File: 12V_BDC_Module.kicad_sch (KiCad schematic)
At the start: 18 parts, among them J1 Conn_01x10_Pin, J2 Conn_01x10_Pin, J4 Conn_01x10_Pin, U1 TPS54531DDA

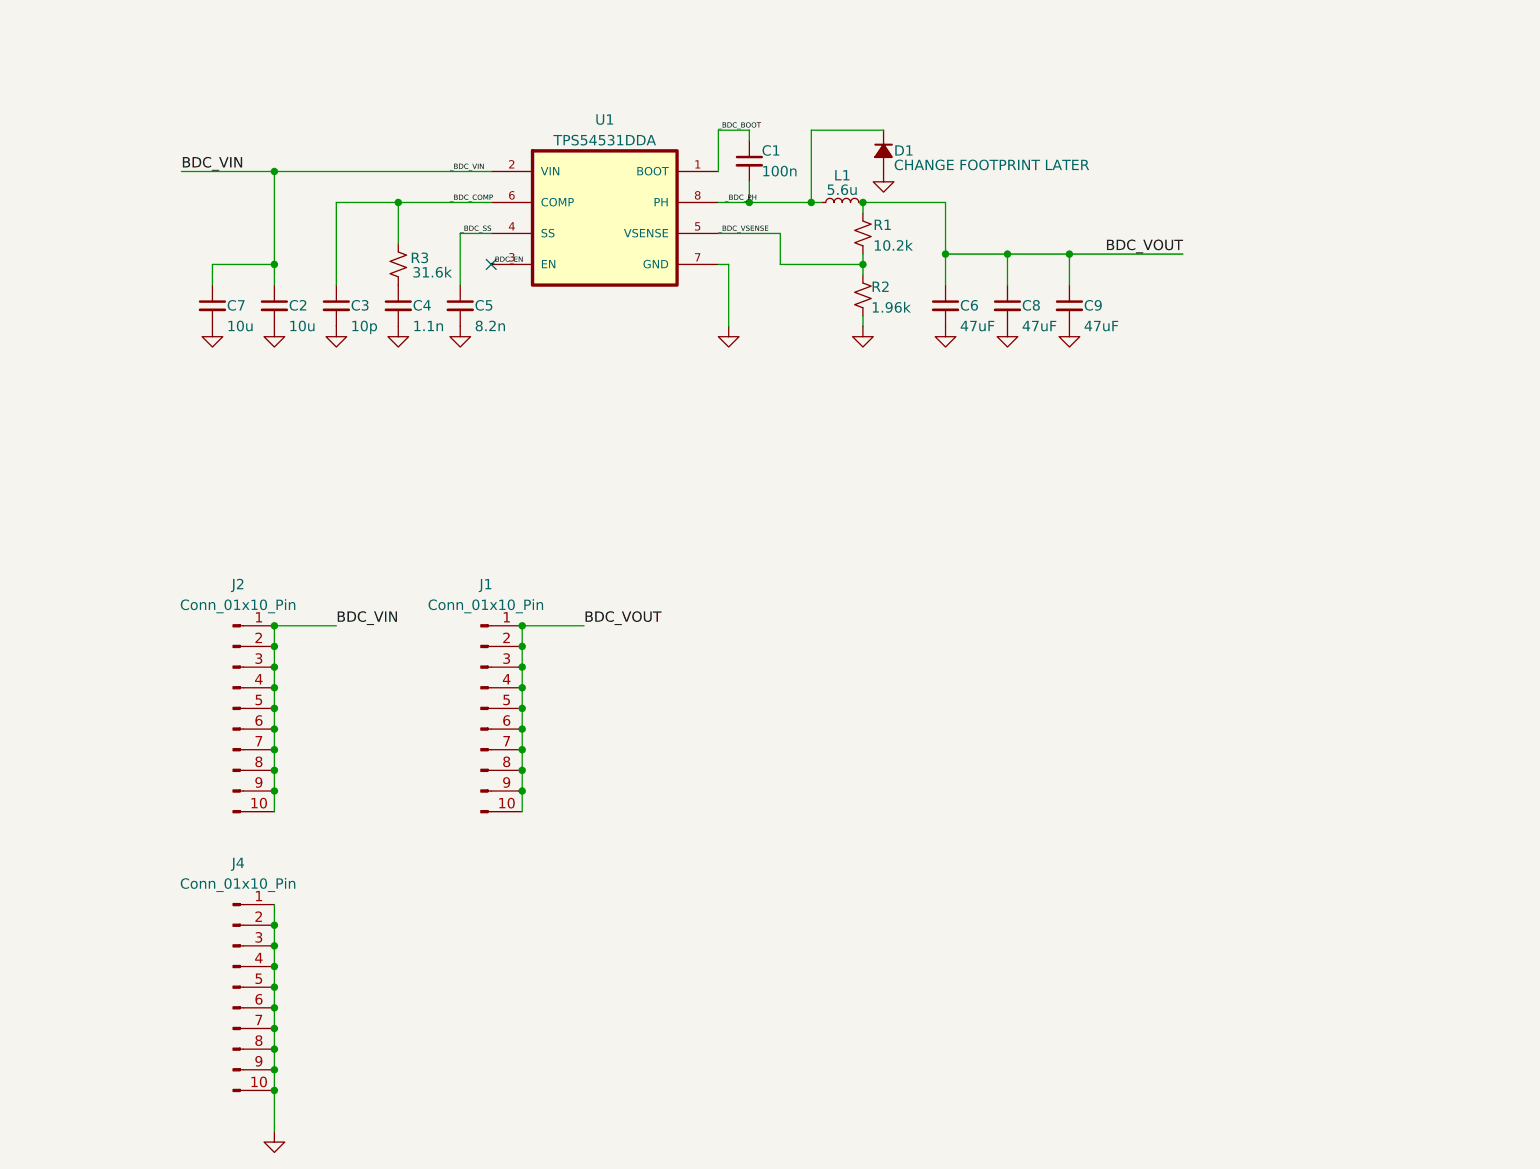
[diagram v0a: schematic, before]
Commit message: Organize, make BDC Module more solderable
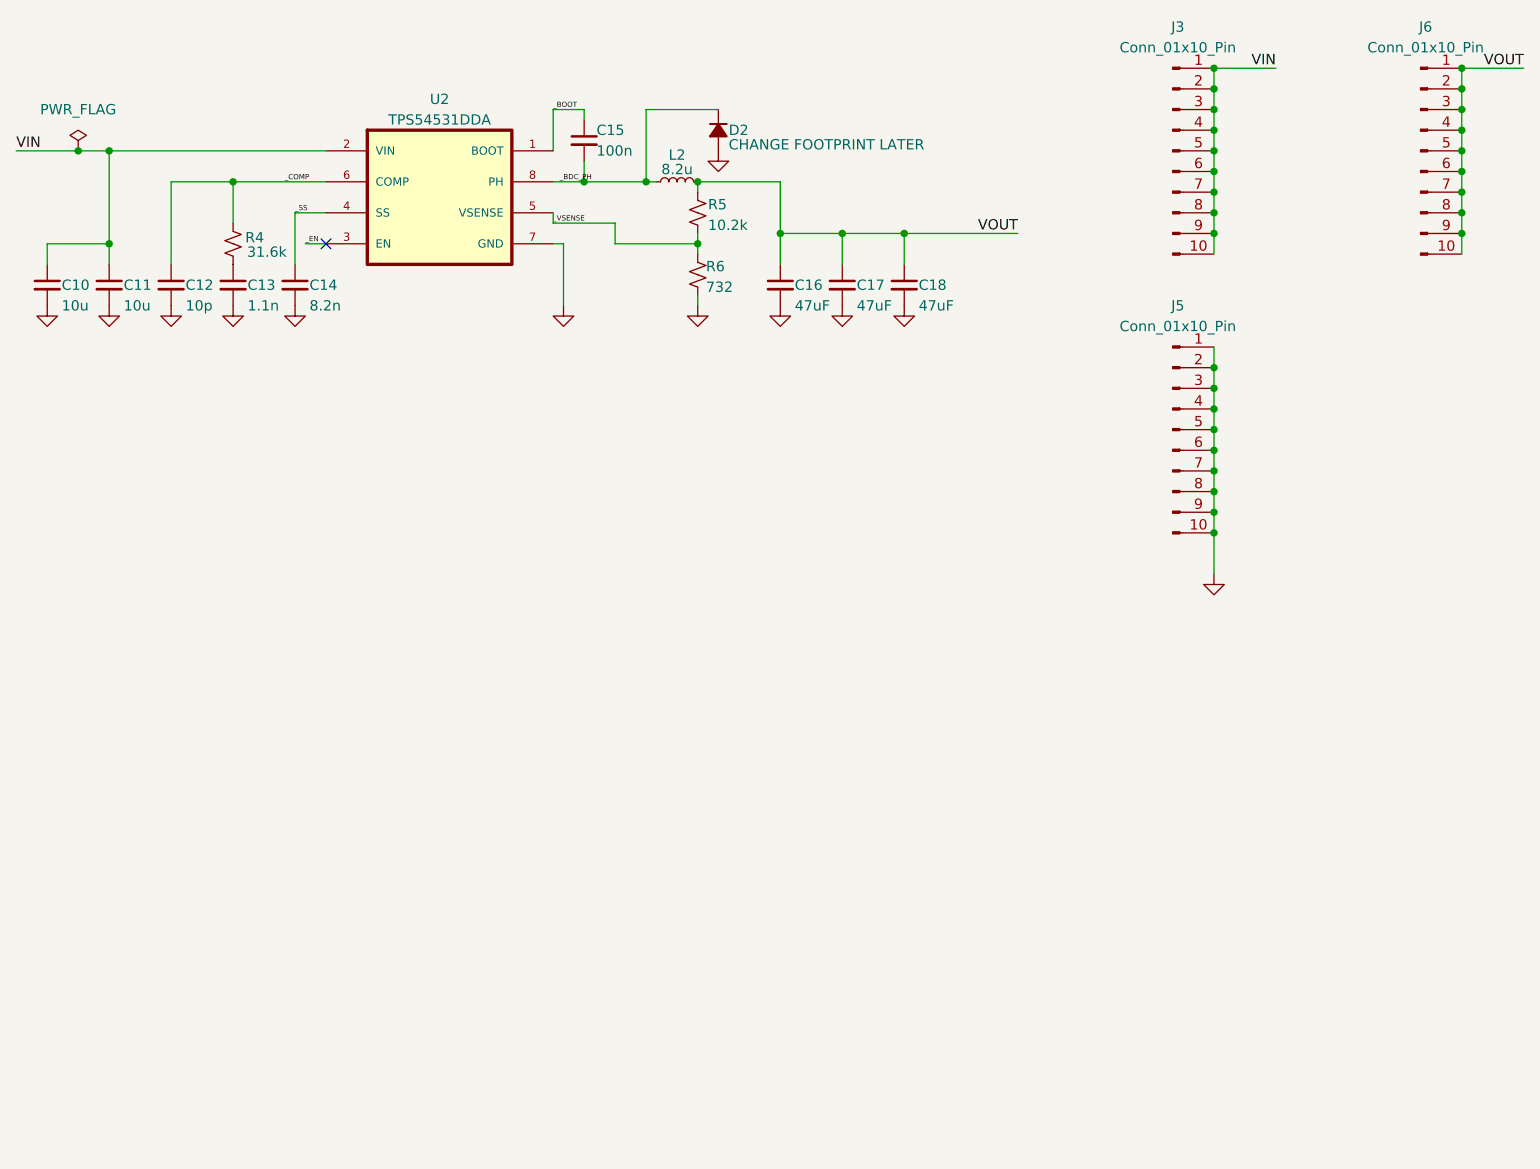
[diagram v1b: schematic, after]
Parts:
- removed C1: 100n, Capacitor_SMD:C_0805_2012Metric, symbol Device:C_Small
- removed C2, C7: 10u, Capacitor_SMD:C_0805_2012Metric, symbol Device:C_Small
- removed C3: 10p, Capacitor_SMD:C_0805_2012Metric, symbol Device:C_Small
- removed C4: 1.1n, Capacitor_SMD:C_0805_2012Metric, symbol Device:C_Small
- removed C5: 8.2n, Capacitor_SMD:C_0805_2012Metric, symbol Device:C_Small
- removed C6, C8, C9: 47uF, Capacitor_SMD:C_0805_2012Metric, symbol Device:C_Small
- removed D1: CHANGE FOOTPRINT LATER, Diode_SMD:D_0805_2012Metric, symbol Device:D_Small_Filled
- removed J1, J2, J4: Conn_01x10_Pin, Connector_PinHeader_2.54mm:PinHeader_1x10_P2.54mm_Vertical, symbol Connector:Conn_01x10_Pin
- removed L1: 5.6u, Inductor_SMD:L_APV_ANR4018, symbol Device:L_Small
- removed R1: 10.2k, Resistor_SMD:R_0805_2012Metric, symbol Device:R_Small_US
- removed R2: 1.96k, Resistor_SMD:R_0805_2012Metric, symbol Device:R_Small_US
- removed R3: 31.6k, Resistor_SMD:R_0805_2012Metric, symbol Device:R_Small_US
- removed U1: TPS54531DDA, footprints:VREG_LM5017MR_NOPB, symbol TPS54531DDA:TPS54531DDA
- added C10, C11: 10u, Capacitor_SMD:C_0805_2012Metric, symbol Device:C_Small
- added C12: 10p, Capacitor_SMD:C_0805_2012Metric, symbol Device:C_Small
- added C13: 1.1n, Capacitor_SMD:C_0805_2012Metric, symbol Device:C_Small
- added C14: 8.2n, Capacitor_SMD:C_0805_2012Metric, symbol Device:C_Small
- added C15: 100n, Capacitor_SMD:C_0805_2012Metric, symbol Device:C_Small
- added C16, C17, C18: 47uF, Capacitor_SMD:C_0805_2012Metric, symbol Device:C_Small
- added D2: CHANGE FOOTPRINT LATER, Diode_SMD:D_0805_2012Metric, symbol Device:D_Small_Filled
- added J3, J5, J6: Conn_01x10_Pin, Connector_PinHeader_2.54mm:PinHeader_1x10_P2.54mm_Vertical, symbol Connector:Conn_01x10_Pin
- added L2: 8.2u, Inductor_SMD:L_APV_ANR4018, symbol Device:L_Small
- added R4: 31.6k, Resistor_SMD:R_0805_2012Metric, symbol Device:R_Small_US
- added R5: 10.2k, Resistor_SMD:R_0805_2012Metric, symbol Device:R_Small_US
- added R6: 732, Resistor_SMD:R_0805_2012Metric, symbol Device:R_Small_US
- added U2: TPS54531DDA, footprints:VREG_LM5017MR_NOPB, symbol TPS54531DDA:TPS54531DDA
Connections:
- net GND: now also C10.2, C11.2, C12.2, C13.2, C14.2, C16.2, C17.2, C18.2, D2.2 (A), J5.1 (Pin_1), J5.10 (Pin_10), J5.2 (Pin_2), J5.3 (Pin_3), J5.4 (Pin_4), J5.5 (Pin_5), J5.6 (Pin_6), J5.7 (Pin_7), J5.8 (Pin_8), J5.9 (Pin_9), R6.2, U2.7 (GND)
- net _BDC_PH: now also C15.2, D2.1 (K), L2.1, U2.8 (PH)
- new net: C13.1, R4.1
- new net VIN: C10.1, C11.1, J3.1 (Pin_1), J3.10 (Pin_10), J3.2 (Pin_2), J3.3 (Pin_3), J3.4 (Pin_4), J3.5 (Pin_5), J3.6 (Pin_6), J3.7 (Pin_7), J3.8 (Pin_8), J3.9 (Pin_9), U2.2 (VIN)
- new net VOUT: C16.1, C17.1, C18.1, J6.1 (Pin_1), J6.10 (Pin_10), J6.2 (Pin_2), J6.3 (Pin_3), J6.4 (Pin_4), J6.5 (Pin_5), J6.6 (Pin_6), J6.7 (Pin_7), J6.8 (Pin_8), J6.9 (Pin_9), L2.2, R5.1
- new net _BOOT: C15.1, U2.1 (BOOT)
- new net _COMP: C12.1, R4.2, U2.6 (COMP)
- new net _EN: U2.3 (EN)
- new net _SS: C14.1, U2.4 (SS)
- new net _VSENSE: R5.2, R6.1, U2.5 (VSENSE)
